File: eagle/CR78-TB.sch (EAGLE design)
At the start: 39 parts, among them Q1 2N3904, Q2 2N3904, Q4 2N3904, Q6 2N3904, Q7 2N3904

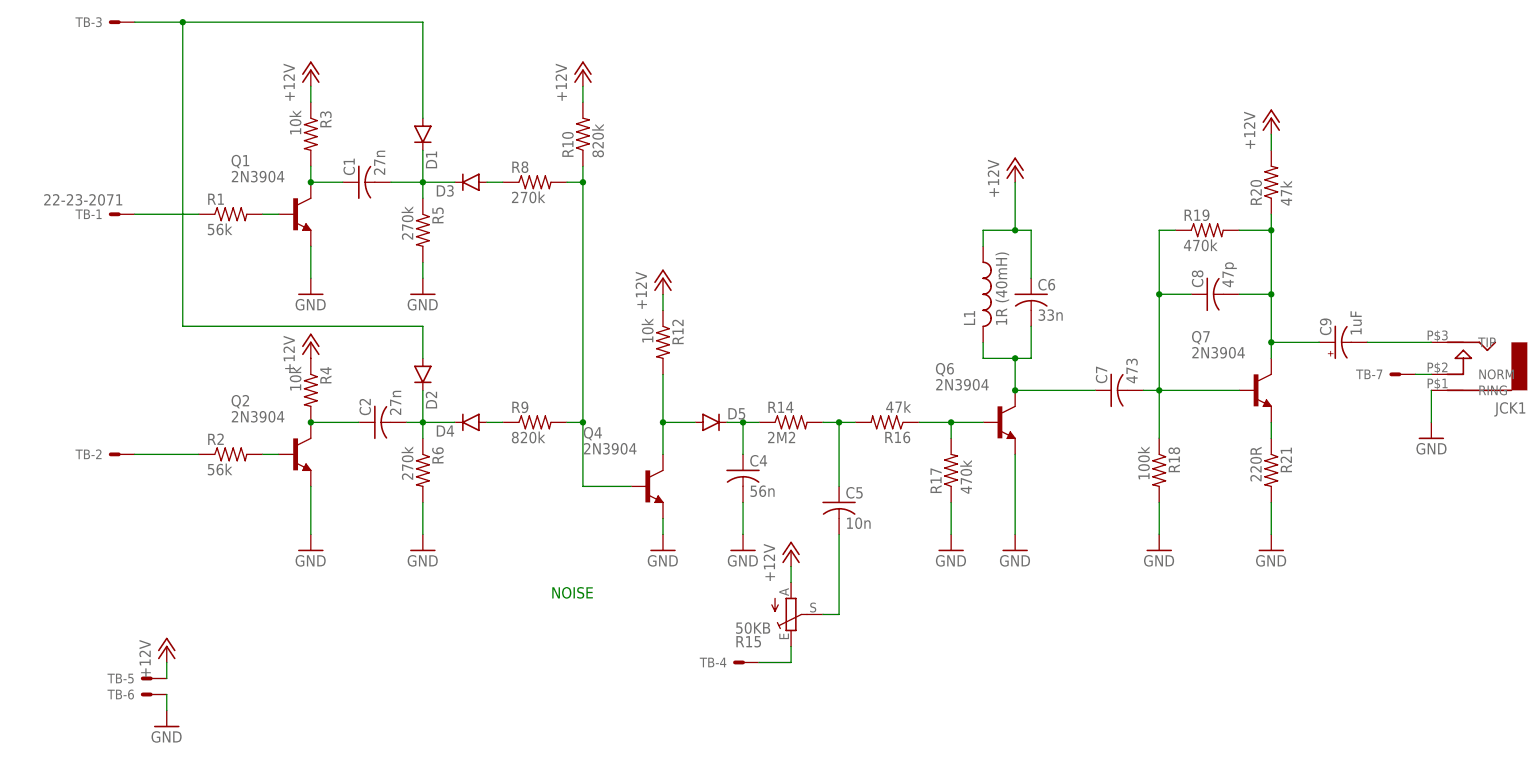
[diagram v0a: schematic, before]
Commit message: rewrote power and ground
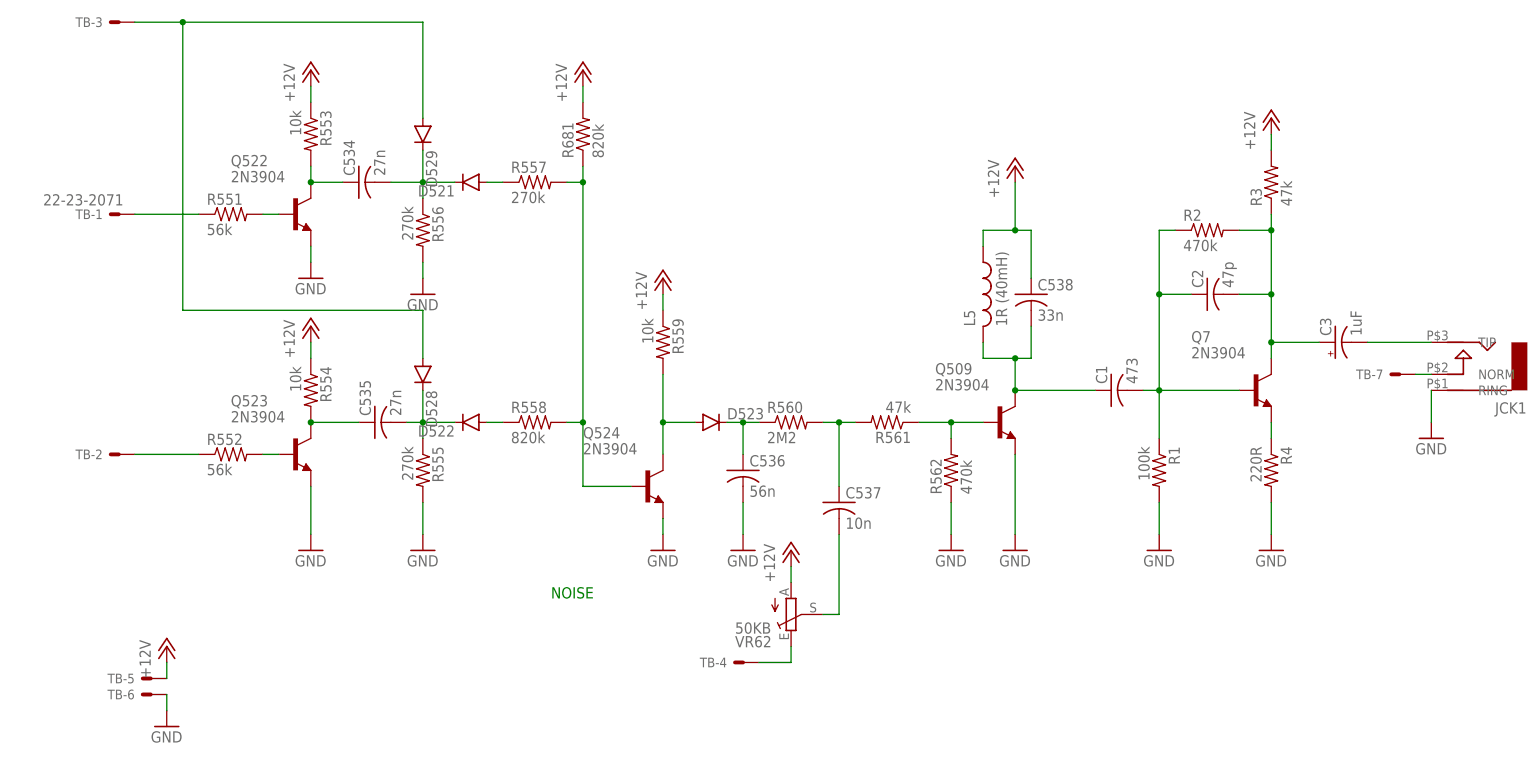
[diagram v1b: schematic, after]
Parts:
- removed C7: 473, rcl:C-US050-025X075
- removed C8: 47p, rcl:C-US050-025X075
- removed R18: 100k, rcl:R-US_0207/7
- removed R19: 470k, rcl:R-US_0207/7
- removed R20: 47k, rcl:R-US_0207/7
- removed R21: 220R, rcl:R-US_0207/7
- added C534, C535: 27n, rcl:C-US050-025X075
- added R551, R552: 56k, rcl:R-US_0207/5V
- added R553: 10k, rcl:R-US_0207/7
- added R554: 10k, rcl:R-US_0207/10
- C1: value 27n -> 473
- C2: value 27n -> 47p
- R1: value 56k -> 100k; device rcl:R-US_0207/5V -> rcl:R-US_0207/7
- R2: value 56k -> 470k; device rcl:R-US_0207/5V -> rcl:R-US_0207/7
- R3: value 10k -> 47k
- R4: value 10k -> 220R; device rcl:R-US_0207/10 -> rcl:R-US_0207/7
- renumbered C4 to C536, C5 to C537, C6 to C538, C9 to C3, D1 to D529, D2 to D528, D3 to D521, D4 to D522, D5 to D523, L1 to L5, Q1 to Q522, Q2 to Q523, Q4 to Q524, Q6 to Q509, R10 to R681, R12 to R559, R14 to R560, R15 to VR62, R16 to R561, R17 to R562, R5 to R556, R6 to R555, R8 to R557, R9 to R558
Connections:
- net +12V: now also R3.2, R553.1, R554.1; no longer R20.2, R3.1, R4.1
- net GND: now also R1.2, R4.2; no longer R18.2, R21.2
- net N$1: now also C535.2; no longer C2.2
- net N$11: now also R552.1; no longer R2.1
- net N$15: now also R4.1; no longer R21.1
- net N$16: now also C2.2, R2.2, R3.1; no longer C8.2, R19.2, R20.1
- net N$18: now also C1.2, C2.1, R1.1, R2.1; no longer C7.2, C8.1, R18.1, R19.1
- net N$20: now also C534.1, R553.2; no longer C1.1, R3.2
- net N$21: now also R551.2; no longer R1.2
- net N$22: now also C534.2; no longer C1.2
- net N$24: now also R551.1; no longer R1.1
- net N$46: now also C535.1, R554.2; no longer C2.1, R4.2
- net N$47: now also R552.2; no longer R2.2
- net N$6: now also C1.1; no longer C7.1
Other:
- moved on the sheet: C1, C2, R1, R2, R3, R4
